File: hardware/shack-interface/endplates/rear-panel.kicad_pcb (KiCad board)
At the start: 2 copper layers, 165 x 51.1 mm, 4 parts

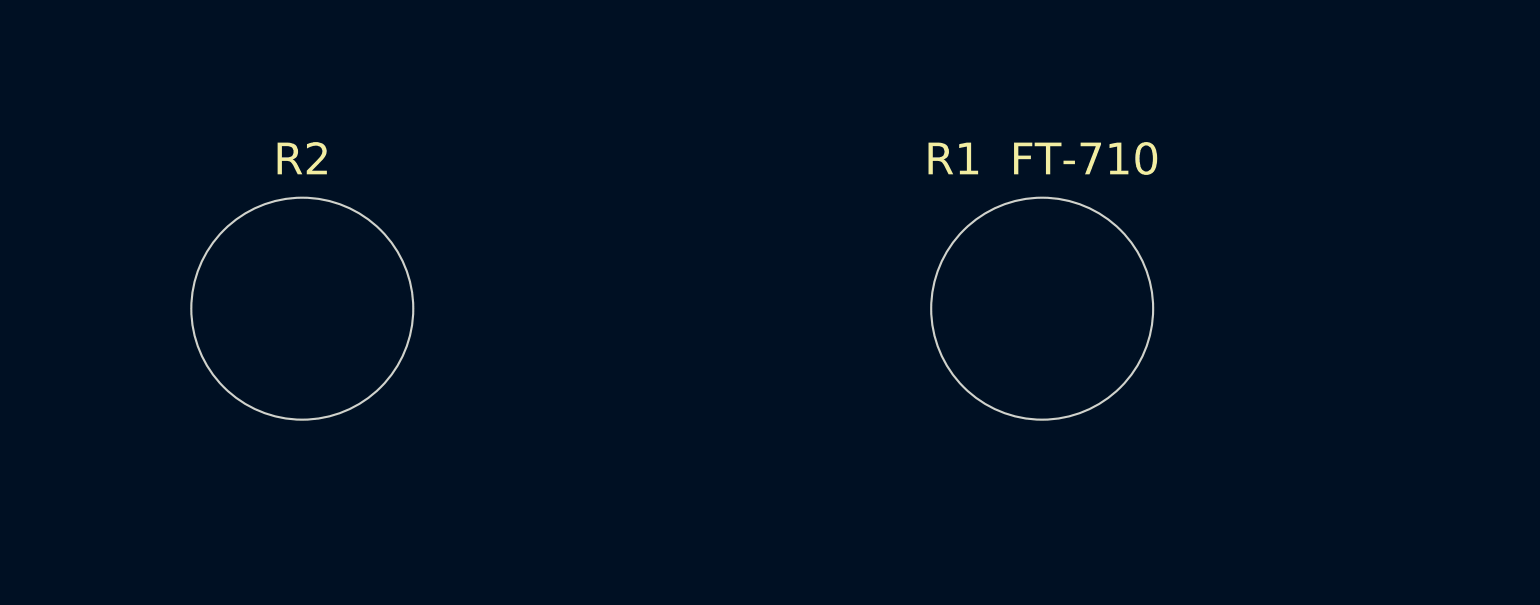
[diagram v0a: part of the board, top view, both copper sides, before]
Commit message: Shack interface: 2 inch display, front plate a8, board p8b, full render
- D-186, M-102: layout p7, J14 (USB-C) at the rear edge; rear plate a7.
- D-187, M-103: Waveshare 2inch LCD (240x320 IPS, ST7789VW); front plate a8;
  new printed display frame on WA-SMSI 9774055151R spacers.
- M-104, M-105: layout p8b with the display notch, routed 155 of 155, DRC 0.
- M-106: full SolidCraft render (case/render-full/); README open-case view.

Co-Authored-By: Claude Opus 5.5 <noreply@anthropic.com>
Claude-Session: https://claude.ai/code/session_01B1V8swdbsr8c87yrmmzj34
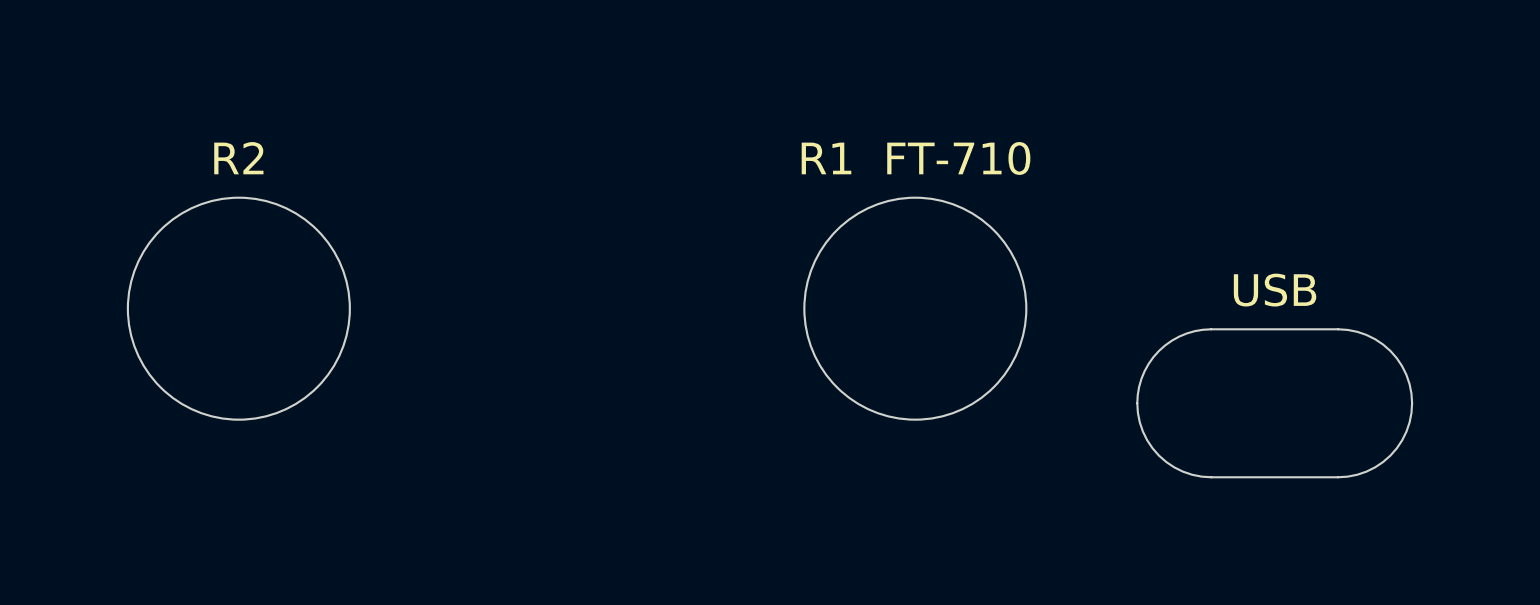
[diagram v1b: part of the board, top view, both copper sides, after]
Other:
- outline, holes or cut-outs redrawn
- board text added: "SRM shack interface rear plate rev A (a8) 2026-10"
- board text added: "USB"
- board text removed: "SRM shack interface rear plate rev A (a3) 2026-10"
